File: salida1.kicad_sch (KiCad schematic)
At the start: 7 parts

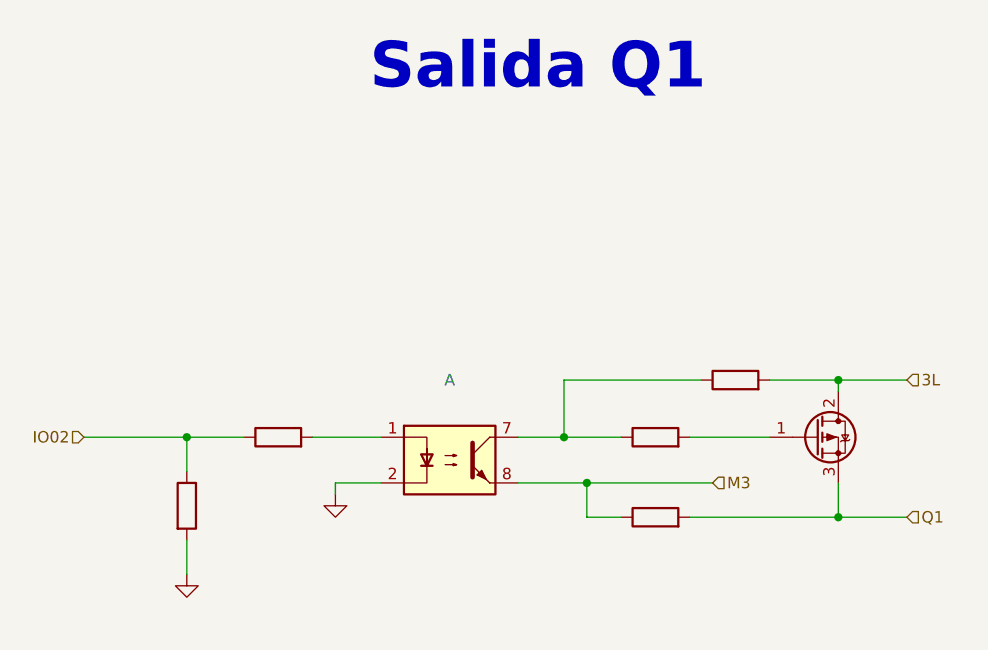
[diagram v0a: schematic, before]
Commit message: add entradas separadas
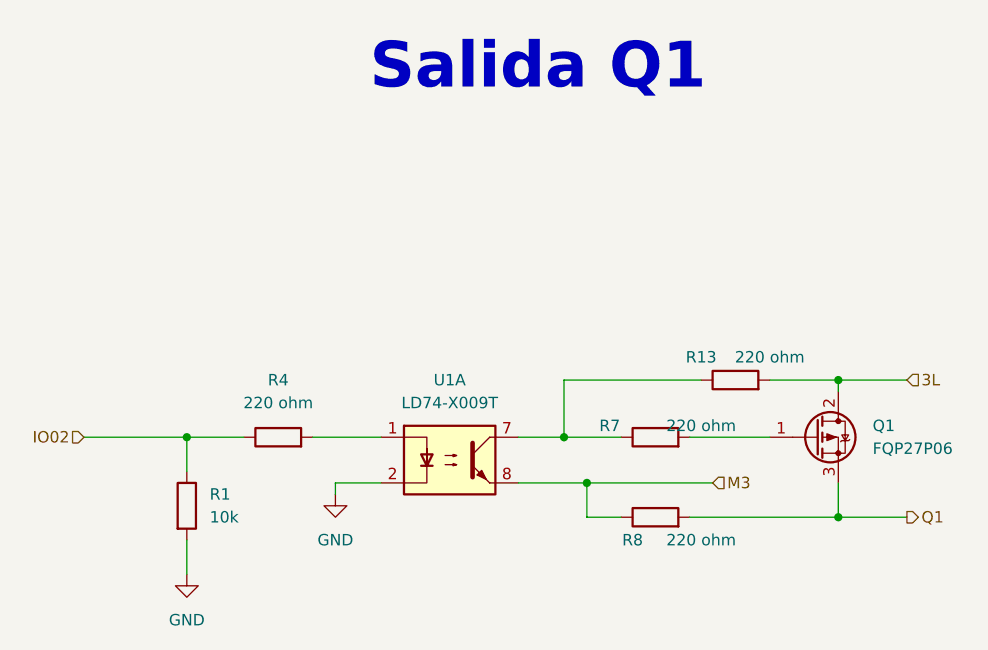
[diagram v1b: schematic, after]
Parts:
- Q1: renamed from ?; value (none) -> FQP27P06; footprint (none) -> Package_TO_SOT_SMD:TO-252-3_TabPin2
- R1: renamed from ?; value (none) -> 10k; footprint (none) -> Resistor_SMD:R_0603_1608Metric
- R13, R4, R7, R8: renamed from ?; value (none) -> 220 ohm; footprint (none) -> Resistor_SMD:R_0603_1608Metric
- U1: renamed from ?; value (none) -> LD74-X009T; footprint (none) -> Package_DIP:DIP-8_W8.89mm_SMDSocket_LongPads
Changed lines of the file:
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@@
-(kicad_sch (version 20220929) (generator eeschema)
+(kicad_sch (version 20221004) (generator eeschema)
   (paper "A4" portrait)
+  (title_block
+    (rev "José Luis Laica")
+  )
   (junction (at 113.03 124.46) (diameter 0) (color 0 0 0 0)
   )
@@
     (effects (font (size 5.08 5.08) (thickness 1.016) bold) (justify left bottom))
   )
-  (hierarchical_label "Q1" (shape input) (at 148.59 128.27 0) (fields_autoplaced)
+  (hierarchical_label "Q1" (shape output) (at 148.59 128.27 0) (fields_autoplaced)
     (effects (font (size 1.27 1.27)) (justify left))
   )
@@
   (symbol (lib_id "Device:R") (at 68.58 127 0) (unit 1)
     (in_bom yes) (on_board yes) (dnp no) (fields_autoplaced)
-    (default_instance (reference "") (unit 1) (value "") (footprint ""))
-    (property "Reference" "" (at 71.12 125.7299 0)
-      (effects (font (size 1.27 1.27)) (justify left))
-    )
-    (property "Value" "" (at 71.12 128.2699 0)
-      (effects (font (size 1.27 1.27)) (justify left))
-    )
-    (property "Footprint" "" (at 66.802 127 90)
+    (property "Reference" "R1" (at 71.12 125.7299 0)
+      (effects (font (size 1.27 1.27)) (justify left))
+    )
+    (property "Value" "10k" (at 71.12 128.2699 0)
+      (effects (font (size 1.27 1.27)) (justify left))
+    )
+    (property "Footprint" "Resistor_SMD:R_0603_1608Metric" (at 66.802 127 90)
       (effects (font (size 1.27 1.27)) hide)
     )
@@
     (pin "1")
     (pin "2")
+    (instances
+      (project "PLC 32 V2"
+        (path "/d17a54f1-6eda-453f-95e1-42a53b02a1c3/ee71d592-407c-4f0c-90d3-cb4773606332"
+          (reference "R1") (unit 1) (value "10k") (footprint "Resistor_SMD:R_0603_1608Metric")
+        )
+      )
+    )
   )
   (symbol (lib_id "Device:R") (at 120.65 128.27 90) (unit 1)
     (in_bom yes) (on_board yes) (dnp no)
-    (default_instance (reference "") (unit 1) (value "") (footprint ""))
-    (property "Reference" "" (at 118.11 130.81 90)
-      (effects (font (size 1.27 1.27)))
-    )
-    (property "Value" "" (at 125.73 130.81 90)
-      (effects (font (size 1.27 1.27)))
-    )
-    (property "Footprint" "" (at 120.65 130.048 90)
+    (property "Reference" "R8" (at 118.11 130.81 90)
+      (effects (font (size 1.27 1.27)))
+    )
+    (property "Value" "220 ohm" (at 125.73 130.81 90)
+      (effects (font (size 1.27 1.27)))
+    )
+    (property "Footprint" "Resistor_SMD:R_0603_1608Metric" (at 120.65 130.048 90)
       (effects (font (size 1.27 1.27)) hide)
     )
@@
     (pin "1")
     (pin "2")
+    (instances
+      (project "PLC 32 V2"
+        (path "/d17a54f1-6eda-453f-95e1-42a53b02a1c3/ee71d592-407c-4f0c-90d3-cb4773606332"
+          (reference "R8") (unit 1) (value "220 ohm") (footprint "Resistor_SMD:R_0603_1608Metric")
+        )
+      )
+    )
   )
   (symbol (lib_id "Device:R") (at 78.74 119.38 90) (unit 1)
     (in_bom yes) (on_board yes) (dnp no) (fields_autoplaced)
-    (default_instance (reference "") (unit 1) (value "") (footprint ""))
-    (property "Reference" "" (at 78.74 113.03 90)
-      (effects (font (size 1.27 1.27)))
-    )
-    (property "Value" "" (at 78.74 115.57 90)
-      (effects (font (size 1.27 1.27)))
-    )
-    (property "Footprint" "" (at 78.74 121.158 90)
+    (property "Reference" "R4" (at 78.74 113.03 90)
+      (effects (font (size 1.27 1.27)))
+    )
+    (property "Value" "220 ohm" (at 78.74 115.57 90)
+      (effects (font (size 1.27 1.27)))
+    )
+    (property "Footprint" "Resistor_SMD:R_0603_1608Metric" (at 78.74 121.158 90)
       (effects (font (size 1.27 1.27)) hide)
     )
@@
     (pin "1")
     (pin "2")
+    (instances
+      (project "PLC 32 V2"
+        (path "/d17a54f1-6eda-453f-95e1-42a53b02a1c3/ee71d592-407c-4f0c-90d3-cb4773606332"
+          (reference "R4") (unit 1) (value "220 ohm") (footprint "Resistor_SMD:R_0603_1608Metric")
+        )
+      )
+    )
   )
   (symbol (lib_id "Device:R") (at 120.65 119.38 90) (unit 1)
     (in_bom yes) (on_board yes) (dnp no)
-    (default_instance (reference "") (unit 1) (value "") (footprint ""))
-    (property "Reference" "" (at 115.57 118.11 90)
-      (effects (font (size 1.27 1.27)))
-    )
-    (property "Value" "" (at 125.73 118.11 90)
-      (effects (font (size 1.27 1.27)))
-    )
-    (property "Footprint" "" (at 120.65 121.158 90)
+    (property "Reference" "R7" (at 115.57 118.11 90)
+      (effects (font (size 1.27 1.27)))
+    )
+    (property "Value" "220 ohm" (at 125.73 118.11 90)
+      (effects (font (size 1.27 1.27)))
+    )
+    (property "Footprint" "Resistor_SMD:R_0603_1608Metric" (at 120.65 121.158 90)
       (effects (font (size 1.27 1.27)) hide)
     )
@@
     (pin "1")
     (pin "2")
+    (instances
+      (project "PLC 32 V2"
+        (path "/d17a54f1-6eda-453f-95e1-42a53b02a1c3/ee71d592-407c-4f0c-90d3-cb4773606332"
+          (reference "R7") (unit 1) (value "220 ohm") (footprint "Resistor_SMD:R_0603_1608Metric")
+        )
+      )
+    )
   )
   (symbol (lib_id "Transistor_FET:FQP27P06") (at 138.43 119.38 0) (unit 1)
     (in_bom yes) (on_board yes) (dnp no) (fields_autoplaced)
-    (default_instance (reference "") (unit 1) (value "") (footprint ""))
-    (property "Reference" "" (at 144.78 118.1099 0)
-      (effects (font (size 1.27 1.27)) (justify left))
-    )
-    (property "Value" "" (at 144.78 120.6499 0)
-      (effects (font (size 1.27 1.27)) (justify left))
-    )
-    (property "Footprint" "" (at 143.51 121.285 0)
+    (property "Reference" "Q1" (at 144.78 118.1099 0)
+      (effects (font (size 1.27 1.27)) (justify left))
+    )
+    (property "Value" "FQP27P06" (at 144.78 120.6499 0)
+      (effects (font (size 1.27 1.27)) (justify left))
+    )
+    (property "Footprint" "Package_TO_SOT_SMD:TO-252-3_TabPin2" (at 143.51 121.285 0)
       (effects (font (size 1.27 1.27) italic) (justify left) hide)
     )
@@
     (pin "2")
     (pin "3")
+    (instances
+      (project "PLC 32 V2"
+        (path "/d17a54f1-6eda-453f-95e1-42a53b02a1c3/ee71d592-407c-4f0c-90d3-cb4773606332"
+          (reference "Q1") (unit 1) (value "FQP27P06") (footprint "Package_TO_SOT_SMD:TO-252-3_TabPin2")
+        )
+      )
+    )
   )
   (symbol (lib_id "Isolator:ILD74") (at 97.79 121.92 0) (unit 1)
     (in_bom yes) (on_board yes) (dnp no) (fields_autoplaced)
-    (default_instance (reference "") (unit 1) (value "") (footprint ""))
-    (property "Reference" "" (at 97.79 113.03 0)
-      (effects (font (size 1.27 1.27)))
-    )
-    (property "Value" "" (at 97.79 115.57 0)
-      (effects (font (size 1.27 1.27)))
-    )
-    (property "Footprint" "" (at 92.71 127 0)
+    (property "Reference" "U1" (at 97.79 113.03 0)
+      (effects (font (size 1.27 1.27)))
+    )
+    (property "Value" "LD74-X009T" (at 97.79 115.57 0)
+      (effects (font (size 1.27 1.27)))
+    )
+    (property "Footprint" "Package_DIP:DIP-8_W8.89mm_SMDSocket_LongPads" (at 92.71 127 0)
       (effects (font (size 1.27 1.27) italic) (justify left) hide)
     )
@@
     (pin "5")
     (pin "6")
+    (instances
+      (project "PLC 32 V2"
+        (path "/d17a54f1-6eda-453f-95e1-42a53b02a1c3/ee71d592-407c-4f0c-90d3-cb4773606332"
+          (reference "U1") (unit 1) (value "LD74-X009T") (footprint "Package_DIP:DIP-8_W8.89mm_SMDSocket_LongPads")
+        )
+      )
+    )
   )
   (symbol (lib_id "Device:R") (at 129.54 113.03 90) (unit 1)
     (in_bom yes) (on_board yes) (dnp no)
-    (default_instance (reference "") (unit 1) (value "") (footprint ""))
-    (property "Reference" "" (at 125.73 110.49 90)
-      (effects (font (size 1.27 1.27)))
-    )
-    (property "Value" "" (at 133.35 110.49 90)
-      (effects (font (size 1.27 1.27)))
-    )
-    (property "Footprint" "" (at 129.54 114.808 90)
+    (property "Reference" "R13" (at 125.73 110.49 90)
+      (effects (font (size 1.27 1.27)))
+    )
+    (property "Value" "220 ohm" (at 133.35 110.49 90)
+      (effects (font (size 1.27 1.27)))
+    )
+    (property "Footprint" "Resistor_SMD:R_0603_1608Metric" (at 129.54 114.808 90)
       (effects (font (size 1.27 1.27)) hide)
     )
@@
     (pin "1")
     (pin "2")
+    (instances
+      (project "PLC 32 V2"
+        (path "/d17a54f1-6eda-453f-95e1-42a53b02a1c3/ee71d592-407c-4f0c-90d3-cb4773606332"
+          (reference "R13") (unit 1) (value "220 ohm") (footprint "Resistor_SMD:R_0603_1608Metric")
+        )
+      )
+    )
   )
   (symbol (lib_id "power:GND") (at 68.58 134.62 0) (unit 1)
     (in_bom yes) (on_board yes) (dnp no) (fields_autoplaced)
-    (default_instance (reference "") (unit 1) (value "") (footprint ""))
-    (property "Reference" "" (at 68.58 140.97 0)
-      (effects (font (size 1.27 1.27)) hide)
-    )
-    (property "Value" "" (at 68.58 139.7 0)
+    (property "Reference" "#PWR05" (at 68.58 140.97 0)
+      (effects (font (size 1.27 1.27)) hide)
+    )
+    (property "Value" "GND" (at 68.58 139.7 0)
       (effects (font (size 1.27 1.27)))
     )
@@
     )
     (pin "1")
+    (instances
+      (project "PLC 32 V2"
+        (path "/d17a54f1-6eda-453f-95e1-42a53b02a1c3/ee71d592-407c-4f0c-90d3-cb4773606332"
+          (reference "#PWR05") (unit 1) (value "GND") (footprint "")
+        )
+      )
+    )
   )
   (symbol (lib_id "power:GND") (at 85.09 125.73 0) (unit 1)
     (in_bom yes) (on_board yes) (dnp no) (fields_autoplaced)
-    (default_instance (reference "") (unit 1) (value "") (footprint ""))
-    (property "Reference" "" (at 85.09 132.08 0)
-      (effects (font (size 1.27 1.27)) hide)
-    )
-    (property "Value" "" (at 85.09 130.81 0)
+    (property "Reference" "#PWR08" (at 85.09 132.08 0)
+      (effects (font (size 1.27 1.27)) hide)
+    )
+    (property "Value" "GND" (at 85.09 130.81 0)
       (effects (font (size 1.27 1.27)))
     )
@@
     )
     (pin "1")
+    (instances
+      (project "PLC 32 V2"
+        (path "/d17a54f1-6eda-453f-95e1-42a53b02a1c3/ee71d592-407c-4f0c-90d3-cb4773606332"
+          (reference "#PWR08") (unit 1) (value "GND") (footprint "")
+        )
+      )
+    )
   )
 )

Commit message: input/output separadas
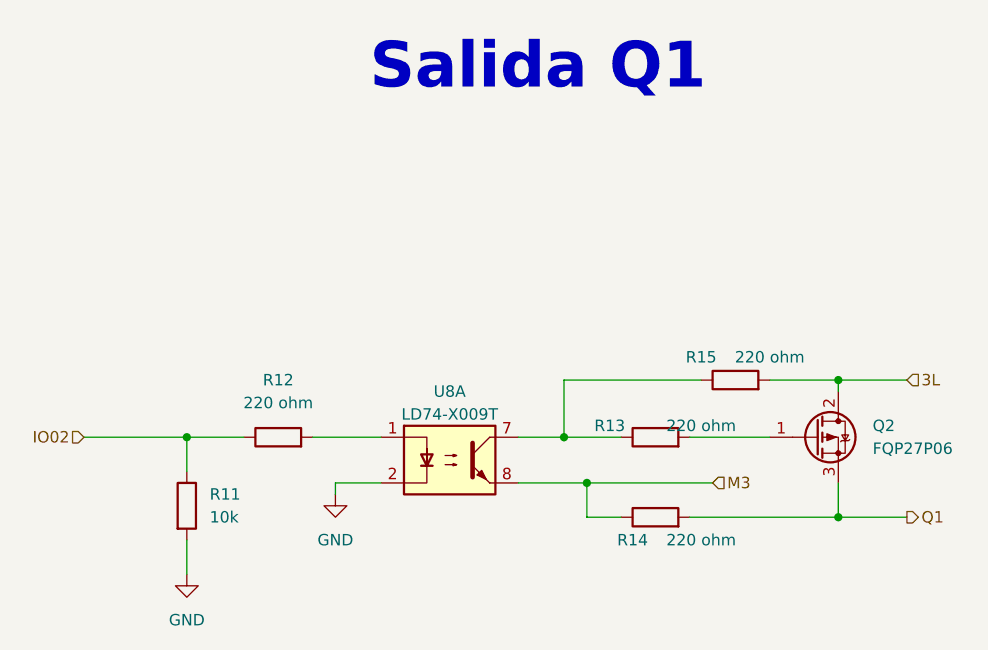
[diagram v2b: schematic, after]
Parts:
- renumbered Q1 to Q2, R1 to R11, R4 to R12, R7 to R13, R8 to R14, R13 to R15, U1 to U8
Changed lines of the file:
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@@
   (paper "A4" portrait)
   (title_block
+    (date "2022-10-09")
     (rev "José Luis Laica")
   )
@@
   (symbol (lib_id "Device:R") (at 68.58 127 0) (unit 1)
     (in_bom yes) (on_board yes) (dnp no) (fields_autoplaced)
-    (property "Reference" "R1" (at 71.12 125.7299 0)
+    (property "Reference" "R11" (at 71.12 125.7299 0)
       (effects (font (size 1.27 1.27)) (justify left))
     )
@@
       (project "PLC 32 V2"
         (path "/d17a54f1-6eda-453f-95e1-42a53b02a1c3/ee71d592-407c-4f0c-90d3-cb4773606332"
-          (reference "R1") (unit 1) (value "10k") (footprint "Resistor_SMD:R_0603_1608Metric")
+          (reference "R11") (unit 1) (value "10k") (footprint "Resistor_SMD:R_0603_1608Metric")
         )
       )
@@
   (symbol (lib_id "Device:R") (at 120.65 128.27 90) (unit 1)
     (in_bom yes) (on_board yes) (dnp no)
-    (property "Reference" "R8" (at 118.11 130.81 90)
+    (property "Reference" "R14" (at 118.11 130.81 90)
       (effects (font (size 1.27 1.27)))
     )
@@
       (project "PLC 32 V2"
         (path "/d17a54f1-6eda-453f-95e1-42a53b02a1c3/ee71d592-407c-4f0c-90d3-cb4773606332"
-          (reference "R8") (unit 1) (value "220 ohm") (footprint "Resistor_SMD:R_0603_1608Metric")
+          (reference "R14") (unit 1) (value "220 ohm") (footprint "Resistor_SMD:R_0603_1608Metric")
         )
       )
@@
   (symbol (lib_id "Device:R") (at 78.74 119.38 90) (unit 1)
     (in_bom yes) (on_board yes) (dnp no) (fields_autoplaced)
-    (property "Reference" "R4" (at 78.74 113.03 90)
+    (property "Reference" "R12" (at 78.74 113.03 90)
       (effects (font (size 1.27 1.27)))
     )
@@
       (project "PLC 32 V2"
         (path "/d17a54f1-6eda-453f-95e1-42a53b02a1c3/ee71d592-407c-4f0c-90d3-cb4773606332"
-          (reference "R4") (unit 1) (value "220 ohm") (footprint "Resistor_SMD:R_0603_1608Metric")
+          (reference "R12") (unit 1) (value "220 ohm") (footprint "Resistor_SMD:R_0603_1608Metric")
         )
       )
@@
   (symbol (lib_id "Device:R") (at 120.65 119.38 90) (unit 1)
     (in_bom yes) (on_board yes) (dnp no)
-    (property "Reference" "R7" (at 115.57 118.11 90)
+    (property "Reference" "R13" (at 115.57 118.11 90)
       (effects (font (size 1.27 1.27)))
     )
@@
       (project "PLC 32 V2"
         (path "/d17a54f1-6eda-453f-95e1-42a53b02a1c3/ee71d592-407c-4f0c-90d3-cb4773606332"
-          (reference "R7") (unit 1) (value "220 ohm") (footprint "Resistor_SMD:R_0603_1608Metric")
+          (reference "R13") (unit 1) (value "220 ohm") (footprint "Resistor_SMD:R_0603_1608Metric")
         )
       )
@@
   (symbol (lib_id "Transistor_FET:FQP27P06") (at 138.43 119.38 0) (unit 1)
     (in_bom yes) (on_board yes) (dnp no) (fields_autoplaced)
-    (property "Reference" "Q1" (at 144.78 118.1099 0)
+    (property "Reference" "Q2" (at 144.78 118.1099 0)
       (effects (font (size 1.27 1.27)) (justify left))
     )
@@
       (project "PLC 32 V2"
         (path "/d17a54f1-6eda-453f-95e1-42a53b02a1c3/ee71d592-407c-4f0c-90d3-cb4773606332"
-          (reference "Q1") (unit 1) (value "FQP27P06") (footprint "Package_TO_SOT_SMD:TO-252-3_TabPin2")
+          (reference "Q2") (unit 1) (value "FQP27P06") (footprint "Package_TO_SOT_SMD:TO-252-3_TabPin2")
         )
       )
@@
   (symbol (lib_id "Isolator:ILD74") (at 97.79 121.92 0) (unit 1)
     (in_bom yes) (on_board yes) (dnp no) (fields_autoplaced)
-    (property "Reference" "U1" (at 97.79 113.03 0)
-      (effects (font (size 1.27 1.27)))
-    )
-    (property "Value" "LD74-X009T" (at 97.79 115.57 0)
+    (property "Reference" "U8" (at 97.79 114.3 0)
+      (effects (font (size 1.27 1.27)))
+    )
+    (property "Value" "LD74-X009T" (at 97.79 116.84 0)
       (effects (font (size 1.27 1.27)))
     )
@@
       (project "PLC 32 V2"
         (path "/d17a54f1-6eda-453f-95e1-42a53b02a1c3/ee71d592-407c-4f0c-90d3-cb4773606332"
-          (reference "U1") (unit 1) (value "LD74-X009T") (footprint "Package_DIP:DIP-8_W8.89mm_SMDSocket_LongPads")
+          (reference "U8") (unit 1) (value "LD74-X009T") (footprint "Package_DIP:DIP-8_W8.89mm_SMDSocket_LongPads")
         )
       )
@@
   (symbol (lib_id "Device:R") (at 129.54 113.03 90) (unit 1)
     (in_bom yes) (on_board yes) (dnp no)
-    (property "Reference" "R13" (at 125.73 110.49 90)
+    (property "Reference" "R15" (at 125.73 110.49 90)
       (effects (font (size 1.27 1.27)))
     )
@@
       (project "PLC 32 V2"
         (path "/d17a54f1-6eda-453f-95e1-42a53b02a1c3/ee71d592-407c-4f0c-90d3-cb4773606332"
-          (reference "R13") (unit 1) (value "220 ohm") (footprint "Resistor_SMD:R_0603_1608Metric")
+          (reference "R15") (unit 1) (value "220 ohm") (footprint "Resistor_SMD:R_0603_1608Metric")
         )
       )
@@
   (symbol (lib_id "power:GND") (at 68.58 134.62 0) (unit 1)
     (in_bom yes) (on_board yes) (dnp no) (fields_autoplaced)
-    (property "Reference" "#PWR05" (at 68.58 140.97 0)
+    (property "Reference" "#PWR012" (at 68.58 140.97 0)
       (effects (font (size 1.27 1.27)) hide)
     )
@@
       (project "PLC 32 V2"
         (path "/d17a54f1-6eda-453f-95e1-42a53b02a1c3/ee71d592-407c-4f0c-90d3-cb4773606332"
-          (reference "#PWR05") (unit 1) (value "GND") (footprint "")
+          (reference "#PWR012") (unit 1) (value "GND") (footprint "")
         )
       )
@@
   (symbol (lib_id "power:GND") (at 85.09 125.73 0) (unit 1)
     (in_bom yes) (on_board yes) (dnp no) (fields_autoplaced)
-    (property "Reference" "#PWR08" (at 85.09 132.08 0)
+    (property "Reference" "#PWR013" (at 85.09 132.08 0)
       (effects (font (size 1.27 1.27)) hide)
     )
@@
       (project "PLC 32 V2"
         (path "/d17a54f1-6eda-453f-95e1-42a53b02a1c3/ee71d592-407c-4f0c-90d3-cb4773606332"
-          (reference "#PWR08") (unit 1) (value "GND") (footprint "")
-        )
-      )
+          (reference "#PWR013") (unit 1) (value "GND") (footprint "")
+        )
+      )
